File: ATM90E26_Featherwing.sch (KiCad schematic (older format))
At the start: 59 parts, among them J1 ST-PJ-312, J2 4P-SMD-2.0-90D, J3 4P-SMD-2.0-90D, J4 12V AC, Q1 8.192MHz, U1 ATM90E26, U2 CJT1117-5.0-SOT223

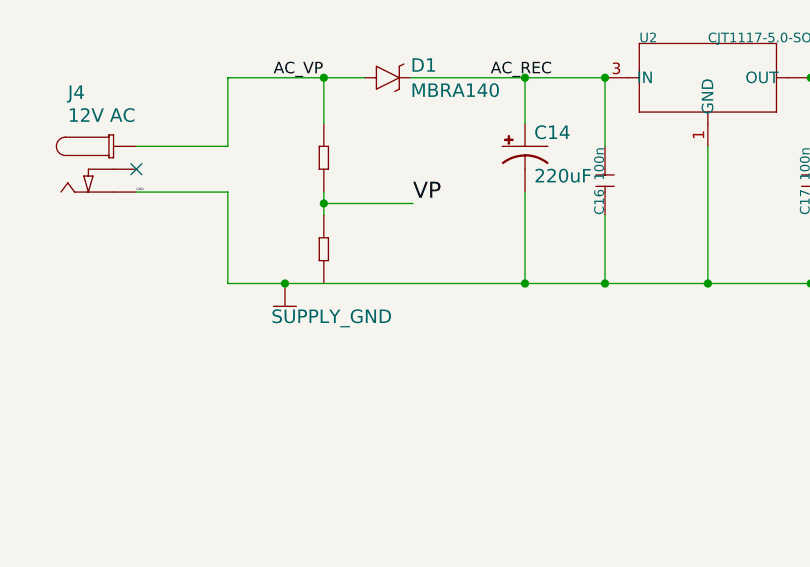
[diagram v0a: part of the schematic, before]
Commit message: Connect R11 to ground
Signed-off-by: Eliot Blennerhassett <eliot@blennerhassett.gen.nz>
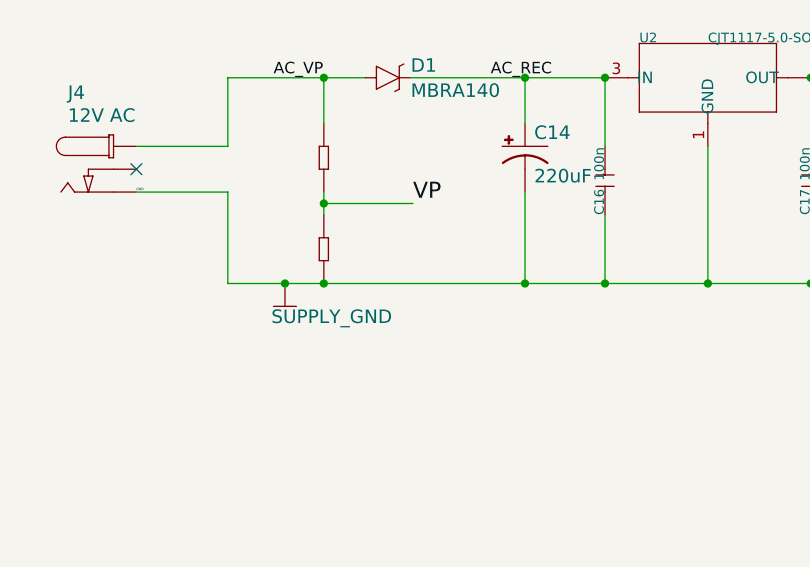
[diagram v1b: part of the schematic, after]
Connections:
- wire segments 205 -> 206
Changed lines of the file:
@@
 Connection ~ 2650 7000
 Wire Wire Line
-	2650 7000 3700 7000
+	2650 7000 2820 7000
 Connection ~ 7100 1850
 Wire Wire Line
@@
 Wire Wire Line
 	9400 3000 9400 3340
+Connection ~ 2820 7000
+Wire Wire Line
+	2820 7000 3700 7000
 $EndSCHEMATC
